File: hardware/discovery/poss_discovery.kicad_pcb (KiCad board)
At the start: 2 copper layers, 96.5 x 66 mm, 110 parts, among them CON1 USB-MICRO-B, SW1 SW_PUSH, SW10 SW_PUSH, SW11 SW_PUSH, SW12 SW_PUSH, SW13 SW_PUSH, SW14 SW_PUSH, SW15 SW_PUSH, SW16 SW_PUSH, SW18 SW_PUSH, SW19 SW_PUSH, SW2 SW_PUSH, SW20 SW_PUSH, SW21 SW_PUSH, SW22 SW_PUSH, SW3 SW_PUSH, SW4 SW_PUSH, SW5 SW_PUSH, SW6 SW_PUSH, SW7 SW_PUSH, SW8 SW_PUSH, SW9 SW_PUSH, U2 MCP73831, U3 BD33IA5, U4 STM32F407VG, U5 SGTL5000, U6 encoder_and_switch, U7 encoder_and_switch, U8 MOLEX_microSD_47219-2001, U9 SSD1306, X1 CRYSTAL

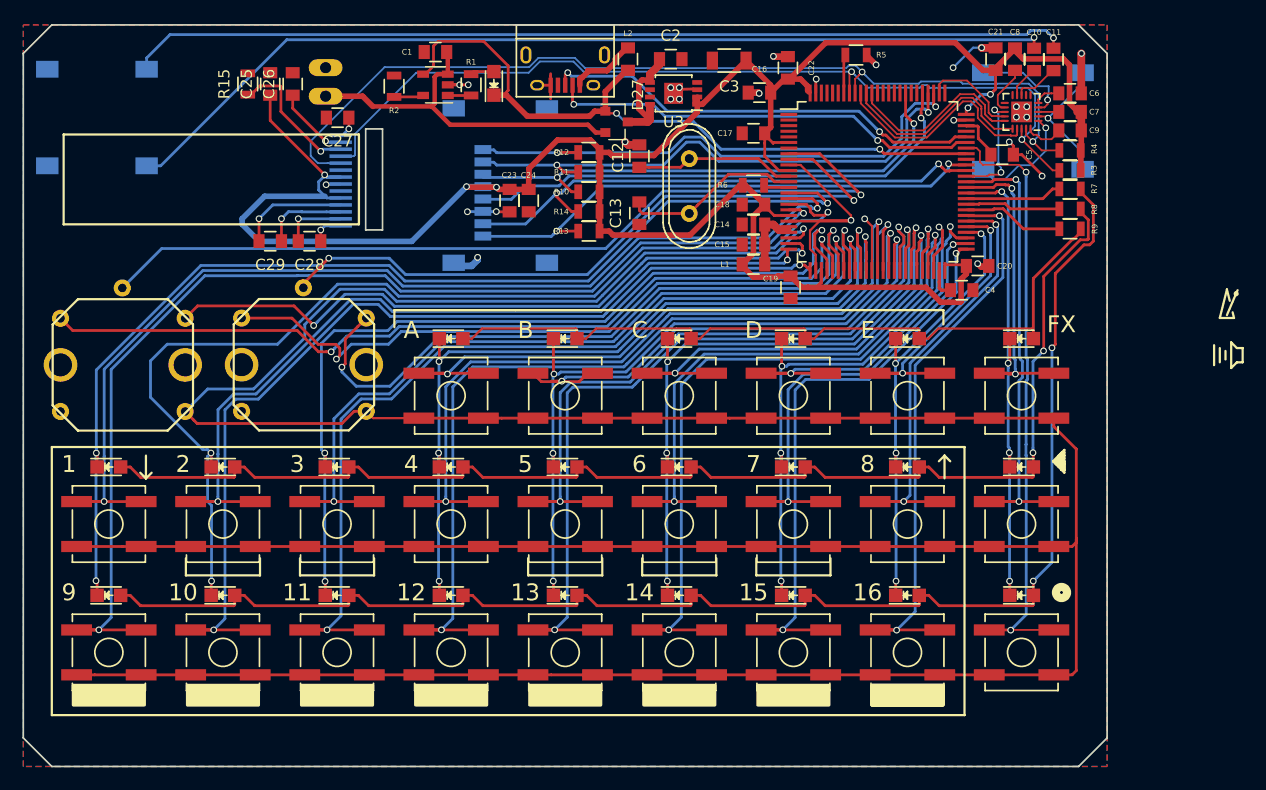
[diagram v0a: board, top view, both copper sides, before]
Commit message: Discovery: Add encoders noise filtering
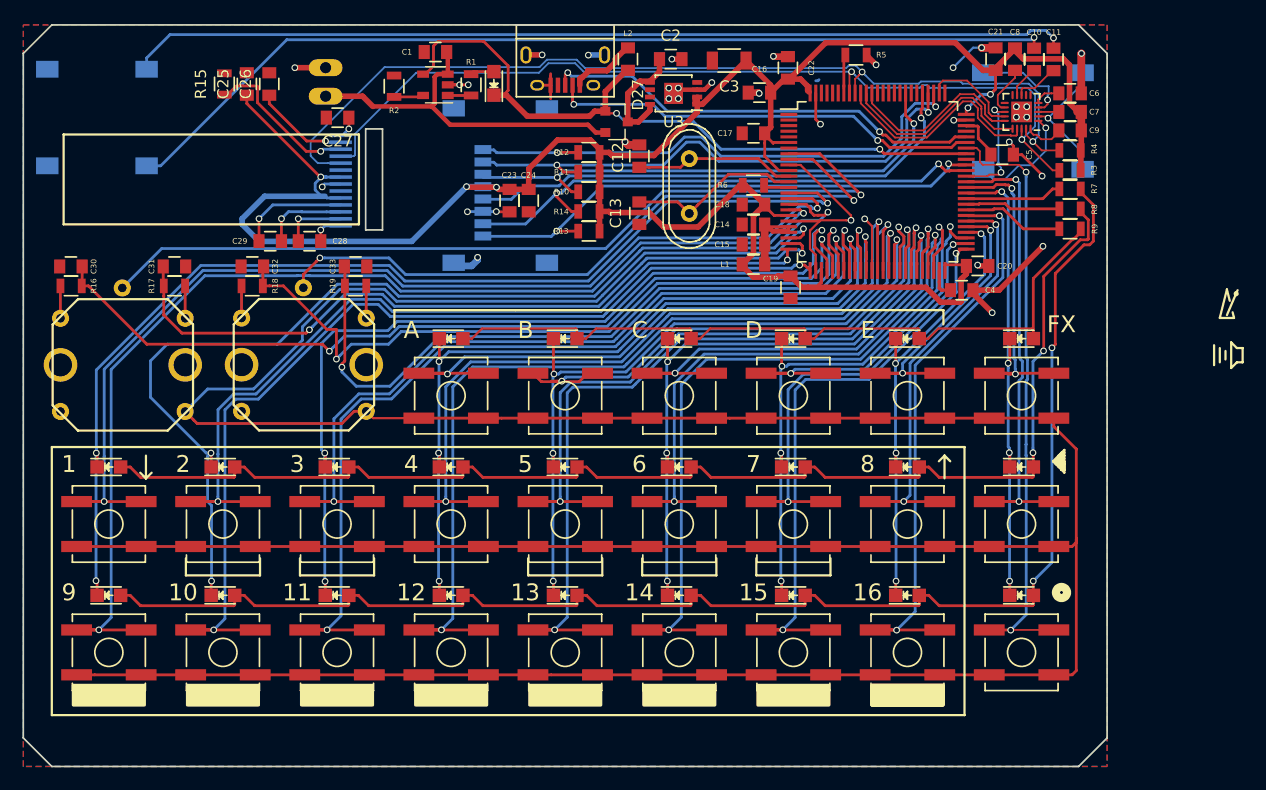
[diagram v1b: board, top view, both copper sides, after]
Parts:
- added C30: 0,1uF, Capacitors_SMD:C_0805, F.Cu at (84.3, 100.3)
- added C31: 0,1uF, Capacitors_SMD:C_0805, F.Cu at (93.5, 100.3)
- added C32: 0,1uF, Capacitors_SMD:C_0805, F.Cu at (100.4, 100.3)
- added C33: 0,1uF, Capacitors_SMD:C_0805, F.Cu at (109.6, 100.3)
- added R16: 27K, Resistors_SMD:R_0805, F.Cu at (84.3, 102.0)
- added R17: 27K, Resistors_SMD:R_0805, F.Cu at (93.5, 102.0)
- added R18: 27K, Resistors_SMD:R_0805, F.Cu at (100.4, 102.0)
- added R19: 27K, Resistors_SMD:R_0805, F.Cu at (109.6, 102.0)
- moved C25 2.08 mm to (99.9, 84.0)
- moved C26 2.08 mm to (101.9, 84.0)
- moved R15 2.08 mm to (97.9, 84.0)
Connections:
- U6 pad 1: ENC_1_A -> Net-(R16-Pad1)
- U6 pad 2: ENC_1_B -> Net-(R17-Pad2)
- U7 pad 1: ENC_2_A -> Net-(R18-Pad1)
- U7 pad 2: ENC_2_B -> Net-(R19-Pad2)
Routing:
- net GND: track 61.7 -> 84.0 mm, vias 27 -> 35
- net ENC_1_B: track 61.9 -> 67.9 mm
- net Net-(C14-Pad2): track 5.81 -> 10.3 mm
- net ENC_2_B: track 60.6 -> 64.5 mm
- net Net-(R16-Pad1): track 0.00 -> 2.89 mm
- net Net-(R17-Pad2): track 0.00 -> 2.89 mm
- net Net-(R18-Pad1): track 0.00 -> 2.87 mm
- net Net-(R19-Pad2): track 0.00 -> 2.87 mm
- net Net-(C26-Pad1): track 6.69 -> 8.53 mm
- net Net-(R15-Pad1): track 12.4 -> 14.0 mm
- net ENC_2_A: track 66.1 -> 67.7 mm
- net ENC_1_A: track 77.9 -> 78.9 mm
- net 3V3: track 212.8 -> 213.5 mm
- net (no net): track 0.63 -> 0.33 mm, vias 1 -> 0

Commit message: Discovery: Add debug port and adjust screen position
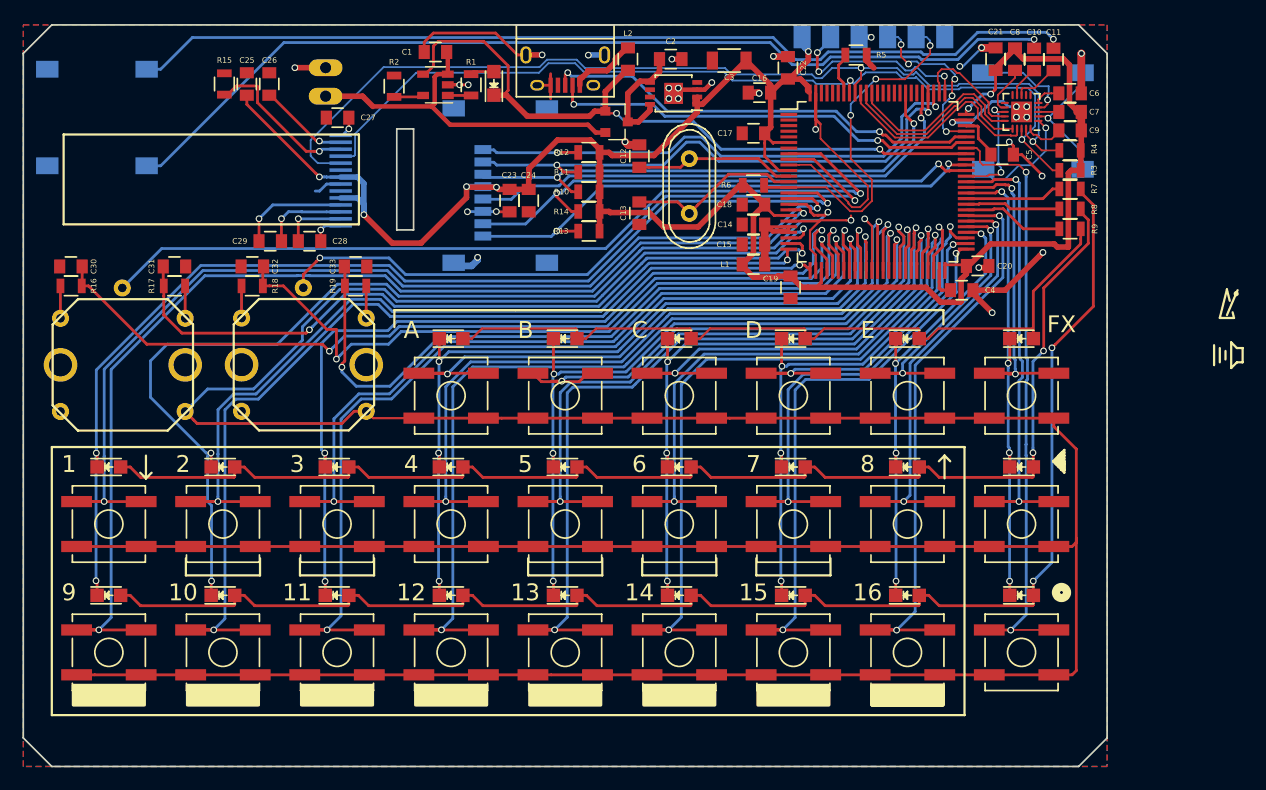
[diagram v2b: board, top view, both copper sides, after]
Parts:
- added U10: STM32_SWD_Connector, stm32f4-disco:STM32_SWD_Connector_SMD, B.Cu at (146.8, 81.3)
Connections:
- net Net-(R6-Pad1) renamed NRST
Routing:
- net GND: track 84.0 -> 116.3 mm, vias 35 -> 34
- net NRST: track 2.51 -> 32.1 mm, vias 0 -> 3
- net SWCLK: track 0.00 -> 17.5 mm, vias 0 -> 3
- net SWDIO: track 0.00 -> 16.2 mm, vias 0 -> 5
- net 3V3: track 213.5 -> 200.6 mm, vias 5 -> 7
- net I2S_LRCLK: track 8.13 -> 10.2 mm
- net Net-(C10-Pad1): track 84.7 -> 86.3 mm
- net Audio_SCL: track 84.4 -> 85.5 mm
- net Net-(C11-Pad1): track 84.0 -> 85.0 mm
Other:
- outline, holes or cut-outs redrawn
- board text added: "GND"
- board text added: "NRST"
- board text added: "SWCLK"
- board text added: "SWDIO"
- board text added: "SWO"
- board text added: "VCC"

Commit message: Discovery: relocation of screen capa and resistor
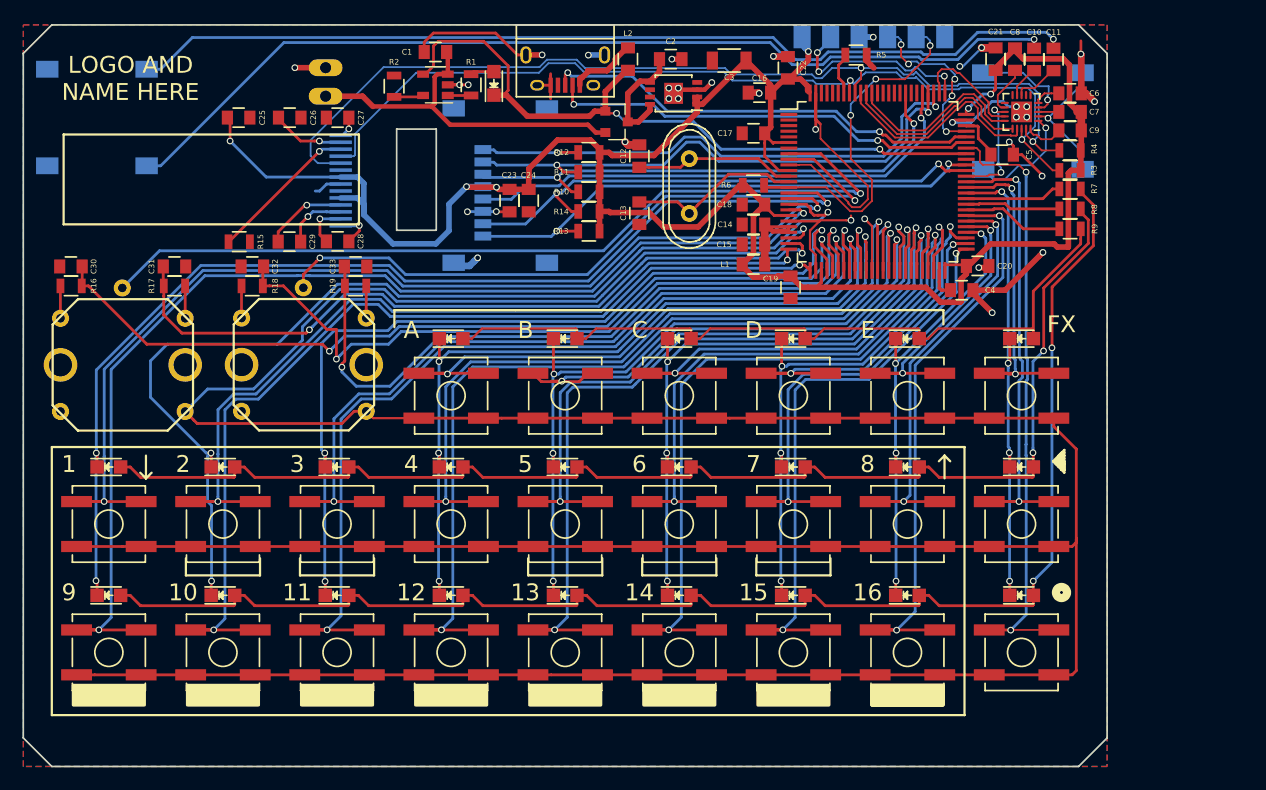
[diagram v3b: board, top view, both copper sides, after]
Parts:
- removed ?: tempo_logo, stm32f4-disco:tempo_logo
- moved R15 14.1 mm to (99.2, 98.0), turned to 0 degrees
- moved C26 3.50 mm to (103.7, 87.0), turned to 0 degrees
- moved C25 3.08 mm to (99.2, 87.0), turned to 0 degrees
- moved C28 2.50 mm to (108.0, 98.0)
- moved C29 1.71 mm to (103.7, 98.0)
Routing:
- net GND: track 116.3 -> 118.9 mm, vias 34 -> 35
- net 3V3: track 200.6 -> 203.0 mm, vias 7 -> 6
- net Net-(C29-Pad2): track 9.78 -> 7.44 mm
- net Net-(C29-Pad1): track 7.54 -> 5.60 mm
- net Net-(C28-Pad2): track 5.78 -> 4.09 mm
- net Net-(C26-Pad1): track 8.09 -> 6.52 mm
- net Net-(R15-Pad1): track 14.0 -> 13.4 mm
- net Net-(C28-Pad1): track 2.93 -> 3.48 mm
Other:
- outline, holes or cut-outs redrawn
- board text added: "LOGO AND NAME HERE"

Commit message: Discovery: Move the screen to the right
and put on connector on the front side.
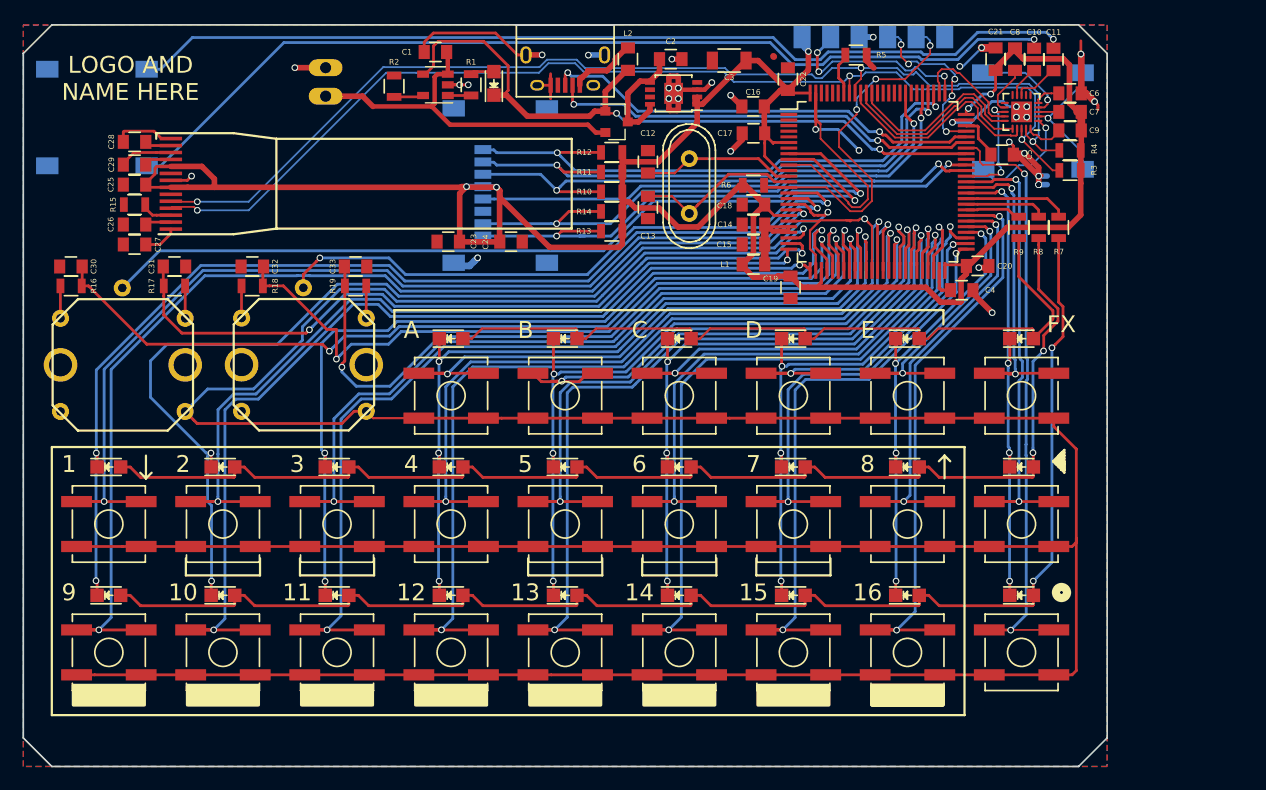
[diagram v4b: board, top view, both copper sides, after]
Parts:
- U9: moved to F.Cu
- moved C27 21.3 mm to (89.9, 98.3)
- moved C28 20.1 mm to (89.9, 89.2), turned to 0 degrees
- moved U9 19.9 mm to (91.9, 97.3)
- moved C26 16.8 mm to (89.9, 96.5), turned to 180 degrees
- moved C29 15.4 mm to (89.9, 91.2), turned to 0 degrees
- moved C25 11.0 mm to (89.9, 93.0), turned to 180 degrees
- moved R15 9.89 mm to (89.9, 94.7), turned to 180 degrees
- moved C23 6.57 mm to (117.9, 98.0), turned to 180 degrees
- moved R9 4.57 mm to (168.7, 96.8), turned to 270 degrees
- moved C24 3.98 mm to (123.4, 98.0), turned to 0 degrees
- moved R7 3.58 mm to (172.2, 96.8), turned to 270 degrees
- moved R8 3.25 mm to (170.4, 96.8), turned to 270 degrees
- moved R10 2.03 mm to (132.4, 93.6)
- moved R11 2.03 mm to (132.4, 91.8)
- moved R12 2.03 mm to (132.4, 90.1)
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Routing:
- net Audio_SDA: track 80.1 -> 96.0 mm, vias 2 -> 3
- net 3V3: track 203.0 -> 216.5 mm, vias 6 -> 5
- net Net-(R15-Pad1): track 13.4 -> 2.85 mm, vias 1 -> 0
- net Audio_SCL: track 85.5 -> 95.9 mm, vias 2 -> 3
- net Net-(D1-Pad2): track 130.3 -> 124.5 mm
- net Net-(C29-Pad2): track 7.44 -> 2.42 mm, vias 1 -> 0
- net Net-(C26-Pad1): track 6.52 -> 2.32 mm, vias 1 -> 0
- net ROW3: track 8.95 -> 4.97 mm
- net GND: track 118.9 -> 122.5 mm
- net Net-(D10-Pad2): track 116.7 -> 113.4 mm
- net SD_CMD: track 46.7 -> 49.5 mm
- net SD_DAT1: track 48.0 -> 50.4 mm
- net SD_DAT2: track 48.1 -> 50.2 mm
- net Net-(C28-Pad1): track 3.48 -> 5.41 mm, vias 1 -> 0
- net Net-(C28-Pad2): track 4.09 -> 2.37 mm, vias 1 -> 0
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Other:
- outline, holes or cut-outs redrawn

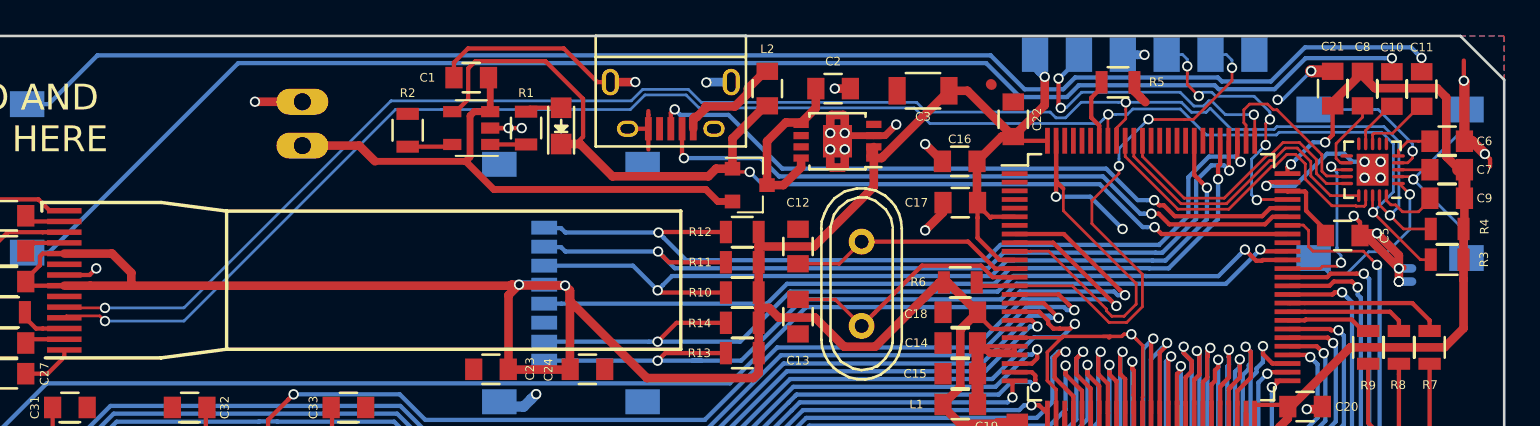
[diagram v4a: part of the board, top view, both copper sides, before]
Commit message: Discovery: Connect VBAT to the MCU
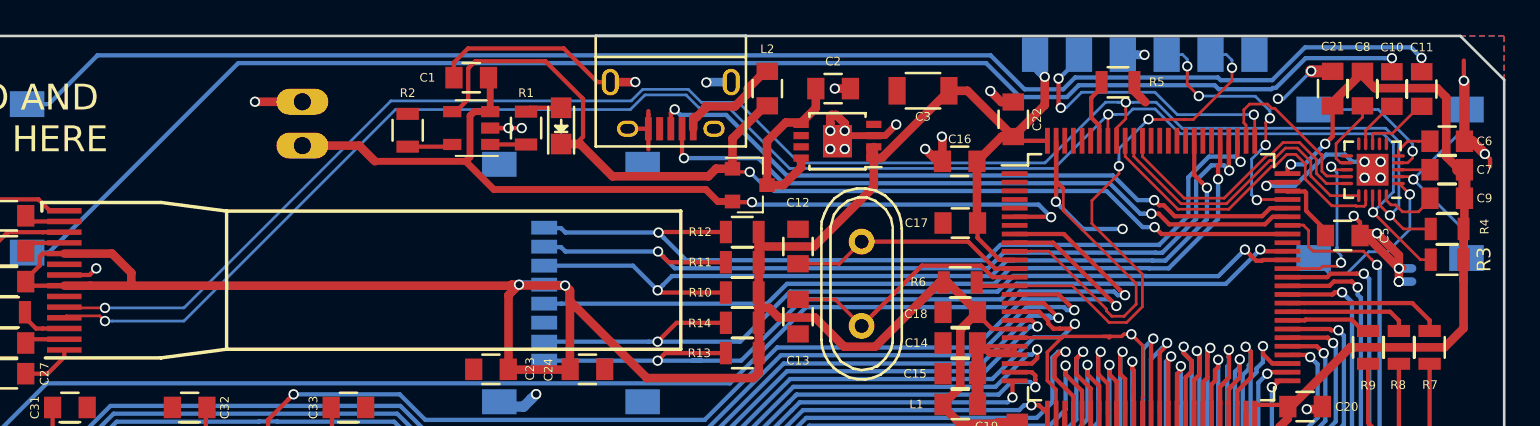
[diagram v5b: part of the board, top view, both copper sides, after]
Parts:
- moved C17 1.18 mm to (145.0, 89.6)
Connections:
- U4 pad 6: 3V3 -> VBAT
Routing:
- net VBAT: track 32.4 -> 53.4 mm, vias 0 -> 2
- net 3V3: track 216.5 -> 214.2 mm
- net Audio_SDA: track 96.0 -> 98.0 mm
- net Audio_SCL: track 95.9 -> 97.7 mm
- net GND: track 122.5 -> 121.1 mm, vias 35 -> 36

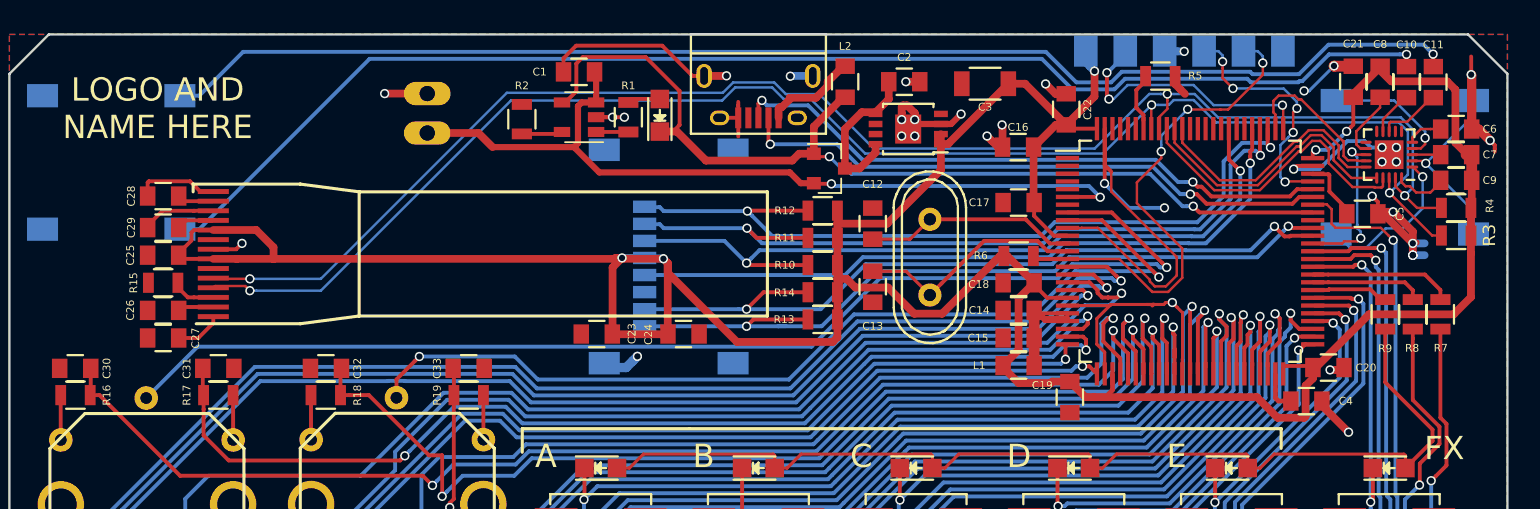
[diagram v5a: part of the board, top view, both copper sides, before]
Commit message: Discovery: Increase all components ref to 0.8 font size
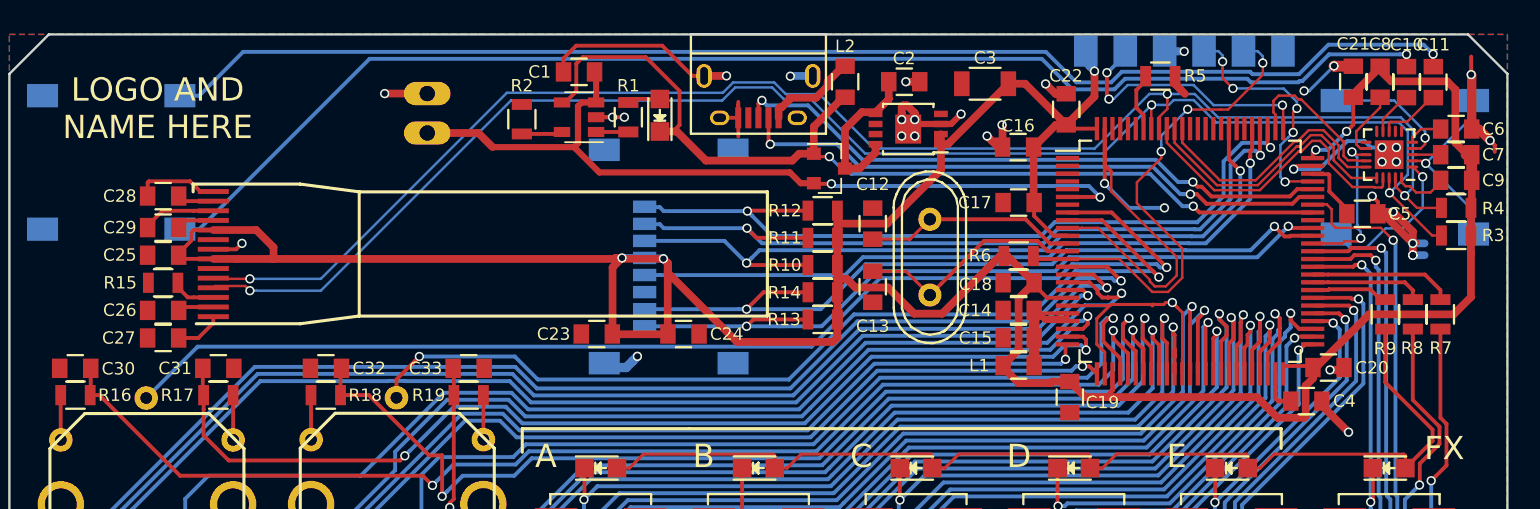
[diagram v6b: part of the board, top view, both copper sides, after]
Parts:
- X1: value CRYSTAL -> 8Mhz
